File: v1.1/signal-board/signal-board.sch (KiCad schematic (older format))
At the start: 38 parts, among them IC1 74HCT245, J1 Jack-DC, J2 02x12 Expansion, J3 JST SM, SW1 SW_MEC_5G, SW2 SW_MEC_5G, U1 TPS63060, U2 ESP32-DEVKITC-32D

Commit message: schematic re-org
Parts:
- removed J2: 02x12 Expansion, symbol Connector_Generic:Conn_02x12_Odd_Even
- added J?: Conn_01x12, symbol Connector_Generic:Conn_01x12
- added J?: Conn_01x16, symbol Connector_Generic:Conn_01x16
- J1: footprint (none) -> Connector_BarrelJack:BarrelJack_CUI_PJ-063AH_Horizontal; DigiKey100 (none) -> 1.03; DigiKeyPN (none) -> CP-063AH-ND; Supplier Part (none) -> PJ-063AH
- gave numbers to parts that had none: 2
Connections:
- net labels added: en, i2c_scl, i2c_sda, io25, io34, io35, sensor_vn, sensor_vp, uart_rx, uart_tx, vspi_clk, vspi_cs, vspi_miso, vspi_mosi
- wire segments 96 -> 95
- no-connect marks 11 -> 8
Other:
- note added: "boot fail if high, internal pull down"
- note added: "en"
- note added: "input pulled up, pwm at boot"
- note added: "io25, DAC_1, ADC8, RTC6"
- note added: "io34, adc6, rtc4"
- note added: "io35, adc7, rtc5"
- note added: "pwm at boot"
- note added: "sensor_vn, io39, adc3, rtc3"
- note added: "sensor_vp, io36, adc0, rtc0"
- note added: "xtal_32k_n"
- note added: "xtal_32k_p"
- moved on the sheet: C1, C10, C2, C4, C6, C7, C8, C9, D1, D2, IC1, J1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

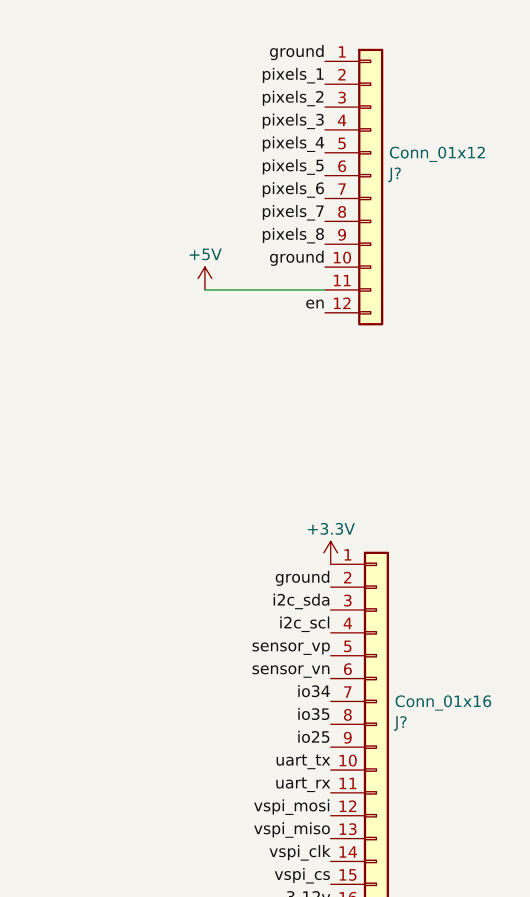
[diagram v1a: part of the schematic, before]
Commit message: footprint updates
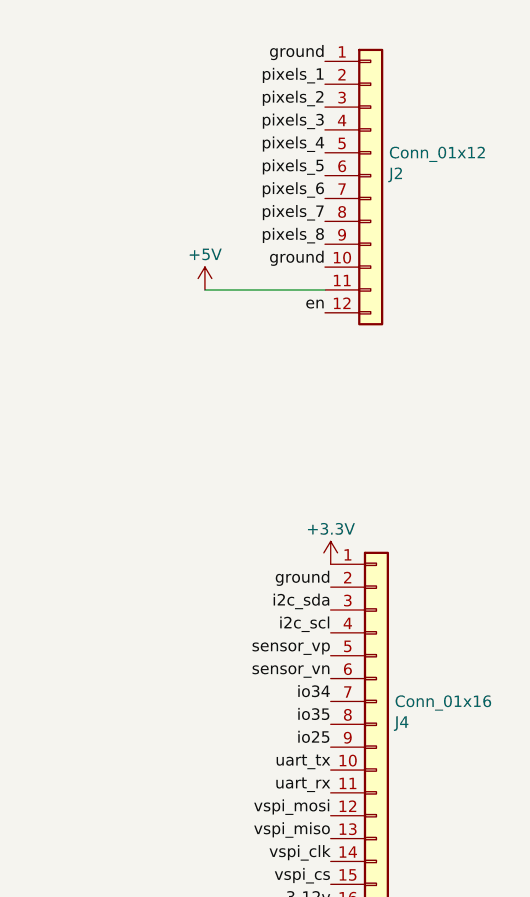
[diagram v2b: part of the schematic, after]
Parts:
- D1, D2: footprint (none) -> LED_THT:LED_D1.8mm_W3.3mm_H2.4mm; Supplier (none) -> temporary footprint - please correct
- IC1: footprint 74HCD245:SOIC-20W_7.5x10.0mm_P1.27mm -> 74HCT245:SOIC-20W_7.5x10.0mm_P1.27mm
- J2: renamed from J?; footprint (none) -> Connector_PinHeader_2.54mm:PinHeader_1x12_P2.54mm_Vertical
- J3: footprint (none) -> jst-landing-pads:jst-smd-landing
- J4: renamed from J?; footprint (none) -> Connector_PinHeader_2.54mm:PinHeader_1x16_P2.54mm_Vertical
- SW1, SW2: footprint PTS525SM15SMTR2LFS:SW_PTS525SM15SMTR2LFS -> PTS 647:PTS647SK38SMTR2LFS; Supplier Part PTS525SM15SMTR2 LFS -> PTS 647 SK70 SMTR2 LFS; digikey part number (none) -> PTS647SK70SMTR2LFSTR
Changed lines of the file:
@@
 3-12v
 $Comp
-L power:+3.3V #PWR?
+L power:+3.3V #PWR0102
 U 1 1 5F4542FA
 P 3275 950
-F 0 "#PWR?" H 3275 800 50  0001 C CNN
+F 0 "#PWR0102" H 3275 800 50  0001 C CNN
 F 1 "+3.3V" H 3275 1103 50  0000 C CNN
 F 2 "" H 3275 950 50  0001 C CNN
@@
 $EndComp
 $Comp
-L power:+3.3V #PWR?
+L power:+3.3V #PWR0103
 U 1 1 5F45397F
 P 3275 2300
-F 0 "#PWR?" H 3275 2150 50  0001 C CNN
+F 0 "#PWR0103" H 3275 2150 50  0001 C CNN
 F 1 "+3.3V" H 3275 2453 50  0000 C CNN
 F 2 "" H 3275 2300 50  0001 C CNN
@@
 $EndComp
 $Comp
-L power:+5V #PWR?
+L power:+5V #PWR0105
 U 1 1 5F3CDD44
 P 11600 2800
-F 0 "#PWR?" H 11600 2650 50  0001 C CNN
+F 0 "#PWR0105" H 11600 2650 50  0001 C CNN
 F 1 "+5V" H 11600 2954 50  0000 C CNN
 F 2 "" H 11600 2800 50  0001 C CNN
@@
 $EndComp
 $Comp
-L power:+3.3V #PWR?
+L power:+3.3V #PWR0101
 U 1 1 5F3CDD55
 P 12150 4000
-F 0 "#PWR?" H 12150 3850 50  0001 C CNN
+F 0 "#PWR0101" H 12150 3850 50  0001 C CNN
 F 1 "+3.3V" H 12150 4153 50  0000 C CNN
 F 2 "" H 12150 4000 50  0001 C CNN
@@
 $EndComp
 $Comp
-L power:GND #PWR?
+L power:GND #PWR0104
 U 1 1 5F3E45C3
 P 2750 5225
-F 0 "#PWR?" H 2750 4975 50  0001 C CNN
+F 0 "#PWR0104" H 2750 4975 50  0001 C CNN
 F 1 "GND" H 2600 5167 50  0000 C CNN
 F 2 "" H 2750 5225 50  0001 C CNN
@@
 F 0 "D1" H 3293 3759 50  0000 C CNN
 F 1 "Red LED" H 3293 3850 50  0000 C CNN
-F 2 "" H 3300 3975 50  0001 C CNN
+F 2 "LED_THT:LED_D1.8mm_W3.3mm_H2.4mm" H 3300 3975 50  0001 C CNN
 F 3 "~" H 3300 3975 50  0001 C CNN
+F 4 "temporary footprint - please correct" H 3300 3975 50  0001 C CNN "Supplier"
 	1    3300 3975
 	1    0    0    -1
@@
 F 0 "D2" H 3293 5009 50  0000 C CNN
 F 1 "Green LED" H 3293 5100 50  0000 C CNN
-F 2 "" H 3300 5225 50  0001 C CNN
+F 2 "LED_THT:LED_D1.8mm_W3.3mm_H2.4mm" H 3300 5225 50  0001 C CNN
 F 3 "~" H 3300 5225 50  0001 C CNN
+F 4 "temporary footprint - please correct" H 3300 5225 50  0001 C CNN "Supplier"
 	1    3300 5225
 	1    0    0    -1
@@
 F 0 "SW2" H 2675 1282 50  0000 C CNN
 F 1 "SW_MEC_5G" H 2675 1157 50  0001 C CNN
-F 2 "PTS525SM15SMTR2LFS:SW_PTS525SM15SMTR2LFS" H 2675 1550 50  0001 C CNN
-F 3 "http://www.apem.com/int/index.php?controller=attachment&id_attachment=488" H 2675 1550 50  0001 C CNN
+F 2 "PTS 647:PTS647SK38SMTR2LFS" H 2675 1550 50  0001 C CNN
+F 3 "https://www.digikey.com/product-detail/en/c-k/PTS-647-SK70-SMTR2-LFS/PTS647SK70SMTR2LFSTR-ND/9649856" H 2675 1550 50  0001 C CNN
 F 4 "digikey" H 2675 1350 50  0001 C CNN "Supplier"
-F 5 "PTS525SM15SMTR2 LFS" H 2675 1350 50  0001 C CNN "Supplier Part"
+F 5 "PTS 647 SK70 SMTR2 LFS" H 2675 1350 50  0001 C CNN "Supplier Part"
+F 6 "PTS647SK70SMTR2LFSTR" H 2675 1350 50  0001 C CNN "digikey part number"
 	1    2675 1350
 	1    0    0    -1
@@
 F 0 "SW1" H 2675 2632 50  0000 C CNN
 F 1 "SW_MEC_5G" H 2675 2507 50  0001 C CNN
-F 2 "PTS525SM15SMTR2LFS:SW_PTS525SM15SMTR2LFS" H 2675 2900 50  0001 C CNN
-F 3 "http://www.apem.com/int/index.php?controller=attachment&id_attachment=488" H 2675 2900 50  0001 C CNN
+F 2 "PTS 647:PTS647SK38SMTR2LFS" H 2675 2900 50  0001 C CNN
+F 3 "https://www.digikey.com/product-detail/en/c-k/PTS-647-SK70-SMTR2-LFS/PTS647SK70SMTR2LFSTR-ND/9649856http://www.apem.com/int/index.php?controller=attachment&id_attachment=488" H 2675 2900 50  0001 C CNN
 F 4 "digikey" H 2675 2700 50  0001 C CNN "Supplier"
-F 5 "PTS525SM15SMTR2 LFS" H 2675 2700 50  0001 C CNN "Supplier Part"
+F 5 "PTS 647 SK70 SMTR2 LFS" H 2675 2700 50  0001 C CNN "Supplier Part"
+F 6 "PTS647SK70SMTR2LFSTR" H 2675 2700 50  0001 C CNN "digikey part number"
 	1    2675 2700
 	1    0    0    -1
@@
 F 0 "J3" H 3480 7508 50  0000 L CNN
 F 1 "JST SM" H 3500 7597 50  0000 L CNN
-F 2 "" H 3400 7500 50  0001 C CNN
+F 2 "jst-landing-pads:jst-smd-landing" H 3400 7500 50  0001 C CNN
 F 3 "~" H 3400 7500 50  0001 C CNN
 	1    3400 7500
@@
 $EndComp
 $Comp
-L Connector_Generic:Conn_01x12 J?
+L Connector_Generic:Conn_01x12 J2
 U 1 1 5F4F1EDA
 P 12325 2300
-F 0 "J?" H 12405 2308 50  0000 L CNN
+F 0 "J2" H 12405 2308 50  0000 L CNN
 F 1 "Conn_01x12" H 12405 2399 50  0000 L CNN
-F 2 "" H 12325 2300 50  0001 C CNN
+F 2 "Connector_PinHeader_2.54mm:PinHeader_1x12_P2.54mm_Vertical" H 12325 2300 50  0001 C CNN
 F 3 "~" H 12325 2300 50  0001 C CNN
 	1    12325 2300
@@
 $EndComp
 $Comp
-L Connector_Generic:Conn_01x16 J?
+L Connector_Generic:Conn_01x16 J4
 U 1 1 5F4F3C58
 P 12350 4700
-F 0 "J?" H 12430 4708 50  0000 L CNN
+F 0 "J4" H 12430 4708 50  0000 L CNN
 F 1 "Conn_01x16" H 12430 4799 50  0000 L CNN
-F 2 "" H 12350 4700 50  0001 C CNN
+F 2 "Connector_PinHeader_2.54mm:PinHeader_1x16_P2.54mm_Vertical" H 12350 4700 50  0001 C CNN
 F 3 "~" H 12350 4700 50  0001 C CNN
 	1    12350 4700
@@
 F 0 "IC1" H 7750 4806 50  0000 C CNN
 F 1 "74HCT245" H 7750 4897 50  0000 C CNN
-F 2 "74HCD245:SOIC-20W_7.5x10.0mm_P1.27mm" H 7750 5575 50  0001 C CNN
+F 2 "74HCT245:SOIC-20W_7.5x10.0mm_P1.27mm" H 7750 5575 50  0001 C CNN
 F 3 "" H 7750 5575 50  0001 C CNN
 F 4 "Digikey" H 7750 5575 50  0001 C CNN "Supplier"

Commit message: layout
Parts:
- added J5, J6: switch_jumpers, Connector_PinHeader_2.54mm:PinHeader_1x02_P2.54mm_Vertical, symbol Connector:Conn_01x02_Female
- renumbered C8 to C10, C4 to C3, C6 to C4, C7 to C5, C9 to C6, C10 to C7, C5 to C8, C3 to C9, R7 to R1, R8 to R2, R9 to R3, R6 to R5, R2 to R6, R3 to R7, R1 to R8, R5 to R9, SW2 to SW1, SW1 to SW2
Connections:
- net +5V: now also J4.15 (Pin_15); no longer J2.11 (Pin_11)
- net GND: now also J2.12 (Pin_12), J2.3 (Pin_3), J4.14 (Pin_14), J5.1 (Pin_1), J6.1 (Pin_1); no longer J2.1 (Pin_1), J2.10 (Pin_10), J4.2 (Pin_2)
- net en: now also J4.2 (Pin_2); no longer J2.12 (Pin_12)
- net i2c_scl: now also J2.1 (Pin_1); no longer J4.4 (Pin_4)
- net i2c_sda: now also J2.2 (Pin_2); no longer J4.3 (Pin_3)
- net io25: now also J4.7 (Pin_7); no longer J4.9 (Pin_9)
- net io34: now also J4.5 (Pin_5); no longer J4.7 (Pin_7)
- net io35: now also J4.6 (Pin_6); no longer J4.8 (Pin_8)
- net level_shift_1: now also U2.15 (IO13); no longer U2.10 (IO26)
- net level_shift_2: now also U2.13 (IO12); no longer U2.11 (IO27)
- net level_shift_3: now also U2.11 (IO27); no longer U2.13 (IO12)
- net level_shift_4: now also U2.10 (IO26); no longer U2.15 (IO13)
- net pixels_1: now also J2.11 (Pin_11); no longer J2.2 (Pin_2)
- net pixels_2: now also J2.10 (Pin_10); no longer J2.3 (Pin_3)
- net pixels_3: now also J2.9 (Pin_9); no longer J2.4 (Pin_4)
- net pixels_4: now also J2.8 (Pin_8); no longer J2.5 (Pin_5)
- net pixels_5: now also J2.7 (Pin_7); no longer J2.6 (Pin_6)
- net pixels_6: now also J2.6 (Pin_6); no longer J2.7 (Pin_7)
- net pixels_7: now also J2.5 (Pin_5); no longer J2.8 (Pin_8)
- net pixels_8: now also J2.4 (Pin_4); no longer J2.9 (Pin_9)
- net sensor_vn: now also J4.4 (Pin_4); no longer J4.6 (Pin_6)
- net sensor_vp: now also J4.3 (Pin_3); no longer J4.5 (Pin_5)
- net uart_rx: now also J4.9 (Pin_9); no longer J4.11 (Pin_11)
- net uart_tx: now also J4.8 (Pin_8); no longer J4.10 (Pin_10)
- net vspi_clk: now also J4.12 (Pin_12); no longer J4.14 (Pin_14)
- net vspi_cs: now also J4.13 (Pin_13); no longer J4.15 (Pin_15)
- net vspi_miso: now also J4.11 (Pin_11); no longer J4.13 (Pin_13)
- net vspi_mosi: now also J4.10 (Pin_10); no longer J4.12 (Pin_12)
- net at R4.1, SW1.3 (B), SW1.4 (B): now also J5.2 (Pin_2)
- net at R6.1, SW2.3 (B), SW2.4 (B): now also J6.2 (Pin_2)
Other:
- moved on the sheet: J2

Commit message: JLC PCB changes
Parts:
- C8, C9: footprint Capacitor_SMD:C_0805_2012Metric_Pad1.15x1.40mm_HandSolder -> Capacitor_SMD:C_0402_1005Metric; LCSC (none) -> C1525
- R10, R11, R12, R13, R14, R15, R16, R17: LCSC (none) -> C17408
- R4, R6: footprint Resistor_SMD:R_0805_2012Metric_Pad1.15x1.40mm_HandSolder -> Resistor_SMD:R_0402_1005Metric; LCSC (none) -> C11702
- R5, R7: footprint Resistor_SMD:R_0805_2012Metric_Pad1.15x1.40mm_HandSolder -> Resistor_SMD:R_0402_1005Metric; LCSC (none) -> C25744
- R8, R9: value 660 -> 680; footprint Resistor_SMD:R_0805_2012Metric_Pad1.15x1.40mm_HandSolder -> Resistor_SMD:R_0402_1005Metric; LCSC (none) -> C25130
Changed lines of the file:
@@
 P 2950 3975
 F 0 "R8" V 3024 3999 50  0000 L CNN
-F 1 "660" V 2876 4001 50  0000 L CNN
-F 2 "Resistor_SMD:R_0805_2012Metric_Pad1.15x1.40mm_HandSolder" H 2950 3975 50  0001 C CNN
+F 1 "680" V 2876 4001 50  0000 L CNN
+F 2 "Resistor_SMD:R_0402_1005Metric" H 2950 3975 50  0001 C CNN
 F 3 "~" H 2950 3975 50  0001 C CNN
 F 4 "Digikey" H 2950 3975 50  0001 C CNN "Supplier"
 F 5 "311-1.00KCRCT-ND" H 2950 3975 50  0001 C CNN "Supplier Part"
+F 6 "C25130" V 2950 3975 50  0001 C CNN "LCSC"
 	1    2950 3975
 	0    1    1    0
@@
 P 2950 5225
 F 0 "R9" V 3024 5249 50  0000 L CNN
-F 1 "660" V 2876 5251 50  0000 L CNN
-F 2 "Resistor_SMD:R_0805_2012Metric_Pad1.15x1.40mm_HandSolder" H 2950 5225 50  0001 C CNN
+F 1 "680" V 2876 5251 50  0000 L CNN
+F 2 "Resistor_SMD:R_0402_1005Metric" H 2950 5225 50  0001 C CNN
 F 3 "~" H 2950 5225 50  0001 C CNN
 F 4 "Digikey" H 2950 5225 50  0001 C CNN "Supplier"
 F 5 "311-1.00KCRCT-ND" H 2950 5225 50  0001 C CNN "Supplier Part"
+F 6 "C25130" V 2950 5225 50  0001 C CNN "LCSC"
 	1    2950 5225
 	0    1    1    0
@@
 F 0 "R4" V 3099 1374 50  0000 L CNN
 F 1 "1k" V 2951 1376 50  0000 L CNN
-F 2 "Resistor_SMD:R_0805_2012Metric_Pad1.15x1.40mm_HandSolder" H 3025 1350 50  0001 C CNN
+F 2 "Resistor_SMD:R_0402_1005Metric" H 3025 1350 50  0001 C CNN
 F 3 "~" H 3025 1350 50  0001 C CNN
 F 4 "Digikey" H 3025 1350 50  0001 C CNN "Supplier"
 F 5 "311-1.00KCRCT-ND" H 3025 1350 50  0001 C CNN "Supplier Part"
+F 6 "C11702" V 3025 1350 50  0001 C CNN "LCSC"
 	1    3025 1350
 	0    -1   -1   0
@@
 F 0 "R6" V 3099 2724 50  0000 L CNN
 F 1 "1k" V 2951 2726 50  0000 L CNN
-F 2 "Resistor_SMD:R_0805_2012Metric_Pad1.15x1.40mm_HandSolder" H 3025 2700 50  0001 C CNN
+F 2 "Resistor_SMD:R_0402_1005Metric" H 3025 2700 50  0001 C CNN
 F 3 "~" H 3025 2700 50  0001 C CNN
 F 4 "Digikey" H 3025 2700 50  0001 C CNN "Supplier"
 F 5 "311-1.00KCRCT-ND" H 3025 2700 50  0001 C CNN "Supplier Part"
+F 6 "C11702" V 3025 2700 50  0001 C CNN "LCSC"
 	1    3025 2700
 	0    -1   -1   0
@@
 F 0 "R5" H 3325 1274 50  0000 L CNN
 F 1 "10k" H 3325 1176 50  0000 L CNN
-F 2 "Resistor_SMD:R_0805_2012Metric_Pad1.15x1.40mm_HandSolder" H 3275 1150 50  0001 C CNN
+F 2 "Resistor_SMD:R_0402_1005Metric" H 3275 1150 50  0001 C CNN
 F 3 "~" H 3275 1150 50  0001 C CNN
 F 4 "Digikey" H 3275 1150 50  0001 C CNN "Supplier"
 F 5 "311-10.0KCRCT-ND" H 3275 1150 50  0001 C CNN "Supplier Part"
+F 6 "C25744" H 3275 1150 50  0001 C CNN "LCSC"
 	1    3275 1150
 	1    0    0    -1
@@
 F 0 "R7" H 3325 2624 50  0000 L CNN
 F 1 "10k" H 3325 2526 50  0000 L CNN
-F 2 "Resistor_SMD:R_0805_2012Metric_Pad1.15x1.40mm_HandSolder" H 3275 2500 50  0001 C CNN
+F 2 "Resistor_SMD:R_0402_1005Metric" H 3275 2500 50  0001 C CNN
 F 3 "~" H 3275 2500 50  0001 C CNN
 F 4 "Digikey" H 3275 2500 50  0001 C CNN "Supplier"
 F 5 "311-10.0KCRCT-ND" H 3275 2500 50  0001 C CNN "Supplier Part"
+F 6 "C25744" H 3275 2500 50  0001 C CNN "LCSC"
 	1    3275 2500
 	1    0    0    -1
@@
 F 4 "Digikey" H 8700 5075 50  0001 C CNN "Supplier"
 F 5 "RC0805FR-07100RL" H 8700 5075 50  0001 C CNN "Supplier Part"
+F 6 "C17408" V 8700 5075 50  0001 C CNN "LCSC"
 	1    8700 5075
 	0    -1   -1   0
@@
 F 4 "Digikey" H 8700 5175 50  0001 C CNN "Supplier"
 F 5 "RC0805FR-07100RL" H 8700 5175 50  0001 C CNN "Supplier Part"
+F 6 "C17408" V 8700 5175 50  0001 C CNN "LCSC"
 	1    8700 5175
 	0    -1   -1   0
@@
 F 4 "Digikey" H 8700 5275 50  0001 C CNN "Supplier"
 F 5 "RC0805FR-07100RL" H 8700 5275 50  0001 C CNN "Supplier Part"
+F 6 "C17408" V 8700 5275 50  0001 C CNN "LCSC"
 	1    8700 5275
 	0    -1   -1   0
@@
 F 4 "Digikey" H 8700 5375 50  0001 C CNN "Supplier"
 F 5 "RC0805FR-07100RL" H 8700 5375 50  0001 C CNN "Supplier Part"
+F 6 "C17408" V 8700 5375 50  0001 C CNN "LCSC"
 	1    8700 5375
 	0    -1   -1   0
@@
 F 4 "Digikey" H 8700 5475 50  0001 C CNN "Supplier"
 F 5 "RC0805FR-07100RL" H 8700 5475 50  0001 C CNN "Supplier Part"
+F 6 "C17408" V 8700 5475 50  0001 C CNN "LCSC"
 	1    8700 5475
 	0    -1   -1   0
@@
 F 4 "Digikey" H 8700 5575 50  0001 C CNN "Supplier"
 F 5 "RC0805FR-07100RL" H 8700 5575 50  0001 C CNN "Supplier Part"
+F 6 "C17408" V 8700 5575 50  0001 C CNN "LCSC"
 	1    8700 5575
 	0    -1   -1   0
@@
 F 4 "Digikey" H 8700 5675 50  0001 C CNN "Supplier"
 F 5 "RC0805FR-07100RL" H 8700 5675 50  0001 C CNN "Supplier Part"
+F 6 "C17408" V 8700 5675 50  0001 C CNN "LCSC"
 	1    8700 5675
 	0    -1   -1   0
@@
 F 4 "Digikey" H 8700 5775 50  0001 C CNN "Supplier"
 F 5 "RC0805FR-07100RL" H 8700 5775 50  0001 C CNN "Supplier Part"
+F 6 "C17408" V 8700 5775 50  0001 C CNN "LCSC"
 	1    8700 5775
 	0    -1   -1   0
@@
 F 0 "C8" H 3135 1537 50  0000 C CNN
 F 1 "0.1µF" H 3475 1532 50  0000 C CNN
-F 2 "Capacitor_SMD:C_0805_2012Metric_Pad1.15x1.40mm_HandSolder" H 3275 1550 50  0001 C CNN
+F 2 "Capacitor_SMD:C_0402_1005Metric" H 3275 1550 50  0001 C CNN
 F 3 "~" H 3275 1550 50  0001 C CNN
 F 4 "Digikey" H 3275 1550 50  0001 C CNN "Supplier"
 F 5 "478-1395-1-ND" H 3275 1550 50  0001 C CNN "Supplier Part"
+F 6 "C1525" H 3275 1550 50  0001 C CNN "LCSC"
 	1    3275 1550
 	1    0    0    -1
@@
 F 0 "C9" H 3135 2887 50  0000 C CNN
 F 1 "0.1µF" H 3475 2882 50  0000 C CNN
-F 2 "Capacitor_SMD:C_0805_2012Metric_Pad1.15x1.40mm_HandSolder" H 3275 2900 50  0001 C CNN
+F 2 "Capacitor_SMD:C_0402_1005Metric" H 3275 2900 50  0001 C CNN
 F 3 "~" H 3275 2900 50  0001 C CNN
 F 4 "Digikey" H 3275 2900 50  0001 C CNN "Supplier"
 F 5 "08055C104KAT2A" H 3275 2900 50  0001 C CNN "Supplier Part"
+F 6 "C1525" H 3275 2900 50  0001 C CNN "LCSC"
 	1    3275 2900
 	1    0    0    -1

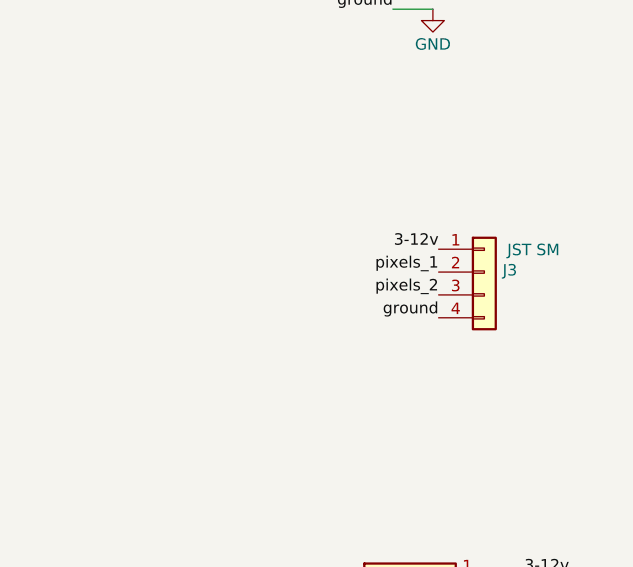
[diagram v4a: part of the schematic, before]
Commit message: updated v1.1 power layout
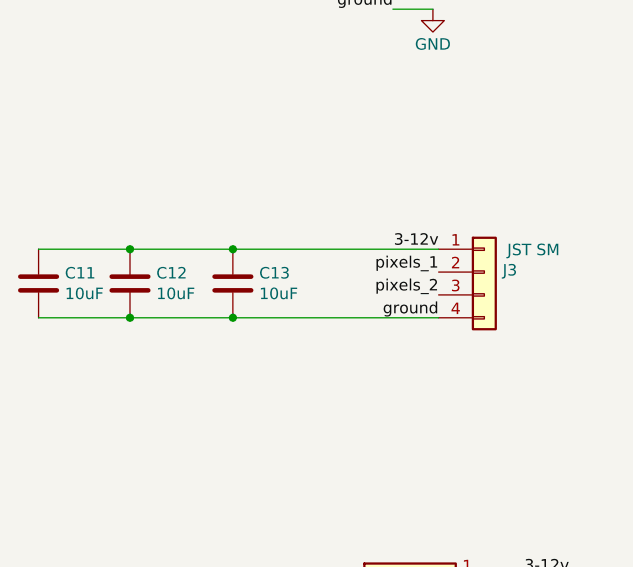
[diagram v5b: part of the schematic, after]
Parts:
- added C11, C12, C13: 10uF, Capacitor_SMD:C_0805_2012Metric_Pad1.15x1.40mm_HandSolder, symbol Device:C
- C1, C2: LCSC (none) -> C90545
- C10: LCSC (none) -> C282736
- C3: footprint Capacitor_SMD:C_0805_2012Metric_Pad1.15x1.40mm_HandSolder -> Capacitor_SMD:C_0402_1005Metric; LCSC (none) -> C1525; Mouser100 0.037 -> (none); MouserPN 80-C0805C104K5RACLR -> (none)
- C4: footprint Capacitor_SMD:C_0805_2012Metric_Pad1.15x1.40mm_HandSolder -> Capacitor_SMD:C_0402_1005Metric; DigiKey100 0.0239 -> (none); DigiKeyPN 1276-2563-1-ND -> (none); LCSC (none) -> C32949; Mouser100 0.04 -> (none); MouserPN 80-C0805C100J3HACTU -> (none); Supplier DigiKey -> (none)
- C5, C6, C7: LCSC (none) -> C45783
- IC1: DigiKey100 (none) -> 0.336; DigiKeyPN (none) -> 296-15849-1-ND; LCSC (none) -> C133641
- R1: footprint Resistor_SMD:R_0805_2012Metric_Pad1.15x1.40mm_HandSolder -> Resistor_SMD:R_0402_1005Metric; DigiKeyPN P123793CT-ND -> (none); LCSC (none) -> C11702; MouserPN 71-CRCW08051K00FKEAC -> (none); Price100 0.039 -> (none)
- R2: footprint Resistor_SMD:R_0805_2012Metric_Pad1.15x1.40mm_HandSolder -> Resistor_SMD:R_0402_1005Metric; DigiKey100 0.0163 -> (none); DigiKeyPN 311-110KCRCT-ND -> (none); LCSC (none) -> C25745; Mouser100 0.019 -> (none); MouserPN 603-RT0805FRE07110RL -> (none); Supplier DigiKey -> (none)
- R3: footprint Resistor_SMD:R_0805_2012Metric_Pad1.15x1.40mm_HandSolder -> Resistor_SMD:R_0402_1005Metric; DigiKey100 0.0163 -> (none); DigiKeyPN 311-1.00MCRCT-ND -> (none); LCSC (none) -> C26083; Mouser100 0.024 -> (none); MouserPN 71-CRCW08051M00FKEAC -> (none); Supplier DigiKey -> (none)
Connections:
- net 3-12v: now also C11.1, C12.1, C13.1
- net GND: now also C11.2, C12.2, C13.2
